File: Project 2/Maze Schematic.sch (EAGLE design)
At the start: 29 parts, among them SW1 BUTTON, SW2 BUTTON, SW3 BUTTON, SW4 BUTTON, SW5 BUTTON, U1 MOD-LED8X8RGB-CONN, U2 MPU-9250, U3 POCKETBEAGLE, U6 MOD-LED8X8RGB-CONN

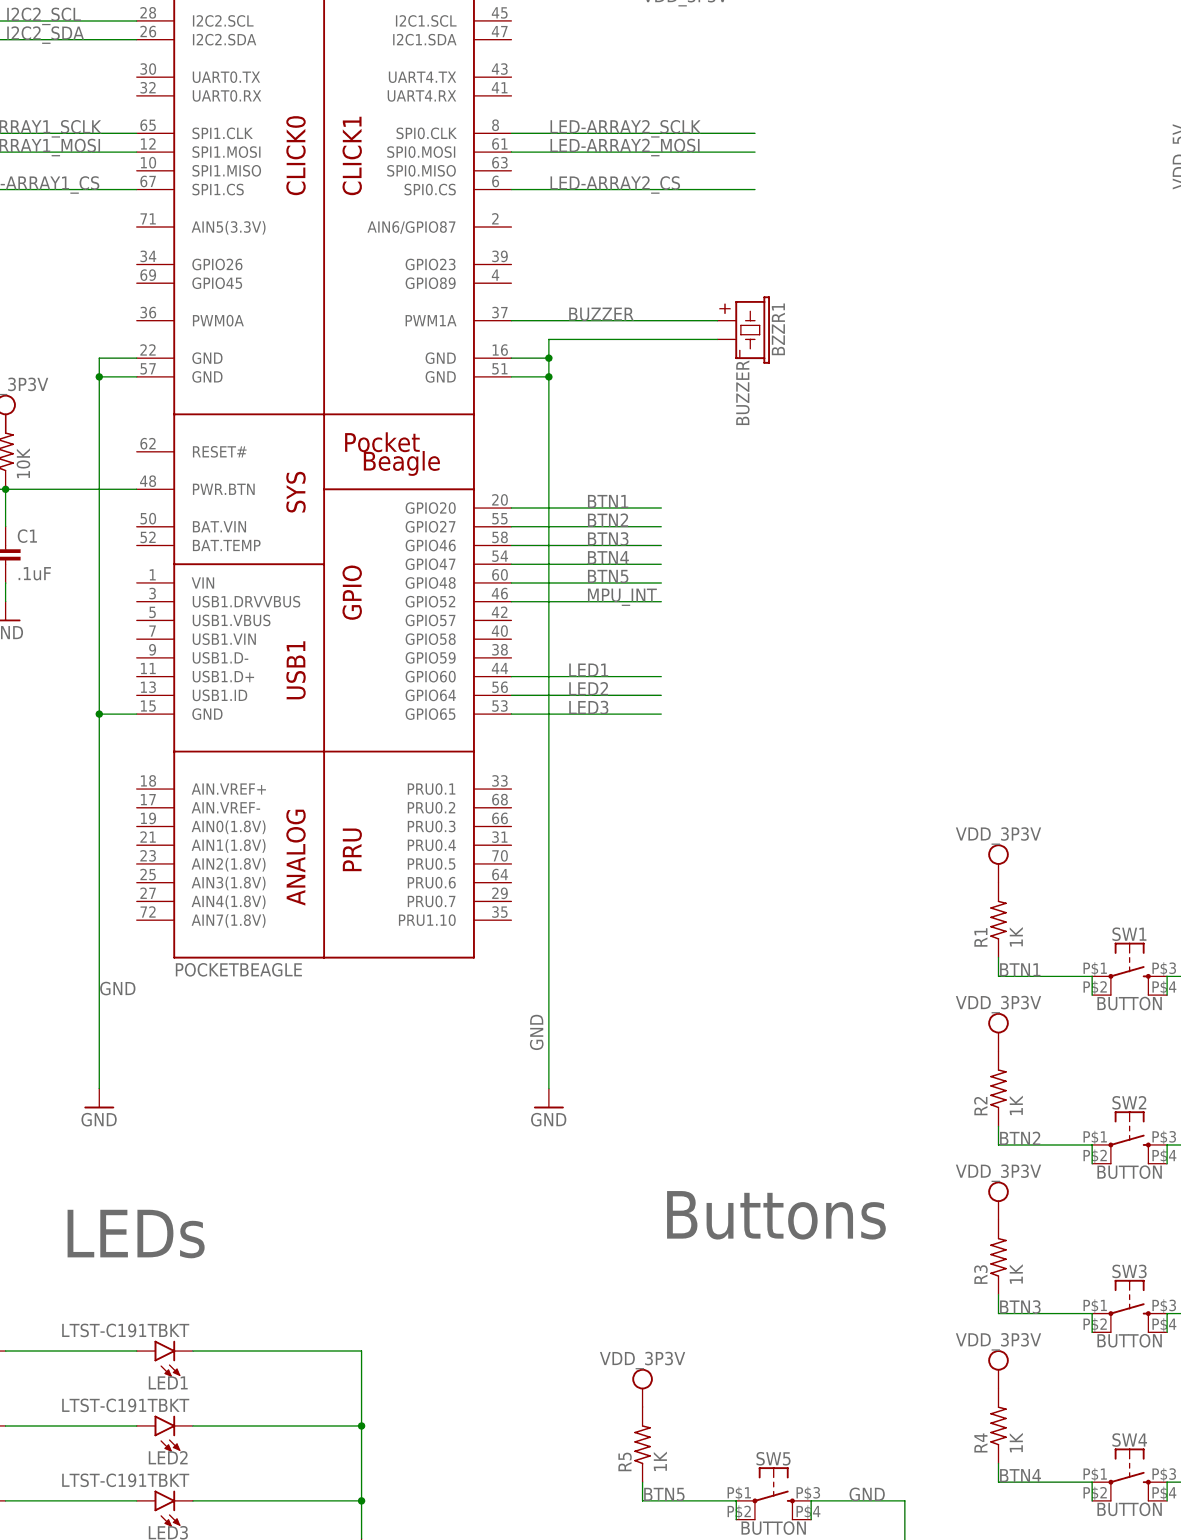
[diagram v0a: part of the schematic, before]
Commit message: Began routing and updated pocket beagle device
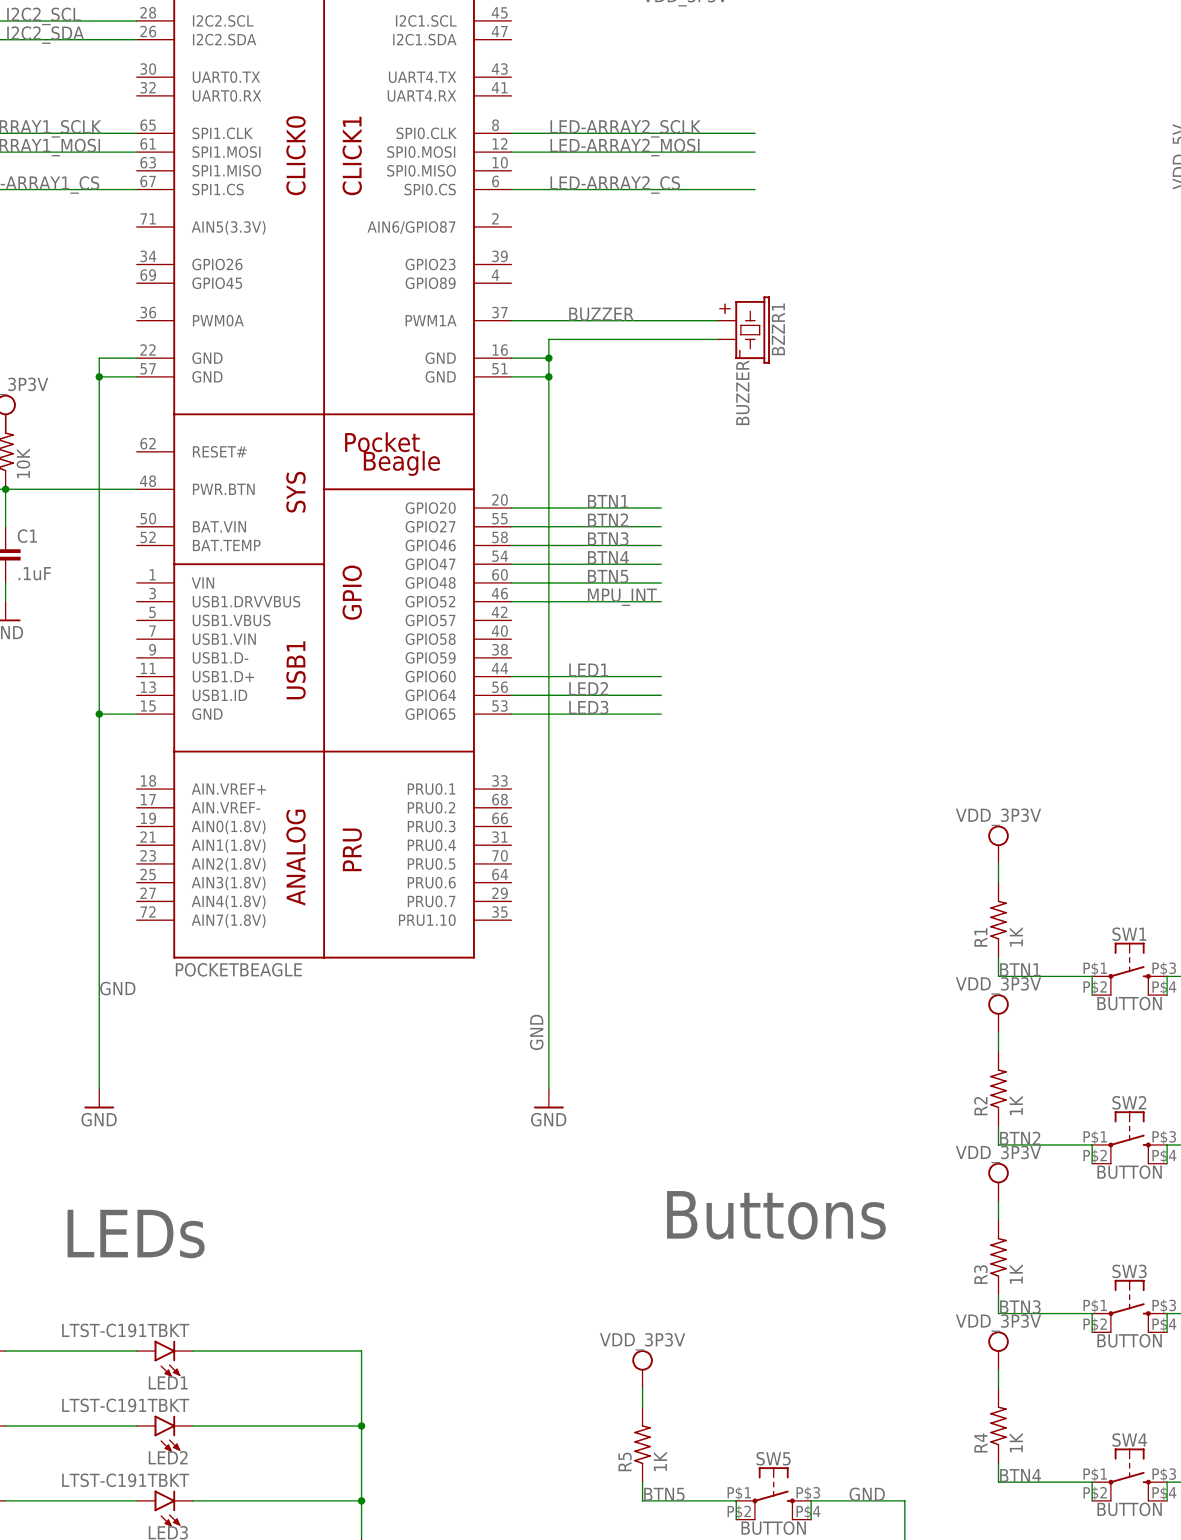
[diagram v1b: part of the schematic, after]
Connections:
- removed net SYS_VDD1_3P3V: R1.2, R2.2, R3.2, R4.2, R5.2
- net VDD_3P3V: now also R1.2, R2.2, R3.2, R4.2, R5.2
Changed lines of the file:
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@@
 <instance part="U6" gate="G$1" x="261.62" y="205.74"/>
 <instance part="GND2" gate="1" x="223.52" y="81.28"/>
-<instance part="SUPPLY2" gate="G$1" x="187.96" y="106.68"/>
+<instance part="SUPPLY2" gate="G$1" x="187.96" y="109.22"/>
 <instance part="SW1" gate="G$1" x="205.74" y="91.44"/>
 <instance part="R1" gate="G$1" x="187.96" y="99.06" rot="R90"/>
 <instance part="GND1" gate="1" x="223.52" y="58.42"/>
-<instance part="SUPPLY1" gate="G$1" x="187.96" y="83.82"/>
+<instance part="SUPPLY1" gate="G$1" x="187.96" y="86.36"/>
 <instance part="SW2" gate="G$1" x="205.74" y="68.58"/>
 <instance part="R2" gate="G$1" x="187.96" y="76.2" rot="R90"/>
 <instance part="GND3" gate="1" x="223.52" y="35.56"/>
-<instance part="SUPPLY3" gate="G$1" x="187.96" y="60.96"/>
+<instance part="SUPPLY3" gate="G$1" x="187.96" y="63.5"/>
 <instance part="SW3" gate="G$1" x="205.74" y="45.72"/>
 <instance part="R3" gate="G$1" x="187.96" y="53.34" rot="R90"/>
 <instance part="GND4" gate="1" x="223.52" y="12.7"/>
-<instance part="SUPPLY4" gate="G$1" x="187.96" y="38.1"/>
+<instance part="SUPPLY4" gate="G$1" x="187.96" y="40.64"/>
 <instance part="SW4" gate="G$1" x="205.74" y="22.86"/>
 <instance part="R4" gate="G$1" x="187.96" y="30.48" rot="R90"/>
 <instance part="GND5" gate="1" x="175.26" y="10.16"/>
-<instance part="SUPPLY5" gate="G$1" x="139.7" y="35.56"/>
+<instance part="SUPPLY5" gate="G$1" x="139.7" y="38.1"/>
 <instance part="SW5" gate="G$1" x="157.48" y="20.32"/>
 <instance part="R5" gate="G$1" x="139.7" y="27.94" rot="R90"/>
@@
 </segment>
 </net>
-<net name="SYS_VDD1_3P3V" class="0">
-<segment>
-<pinref part="SUPPLY2" gate="G$1" pin="SYS_VDD1_3P3V"/>
-<pinref part="R1" gate="G$1" pin="2"/>
-</segment>
-<segment>
-<pinref part="SUPPLY1" gate="G$1" pin="SYS_VDD1_3P3V"/>
-<pinref part="R2" gate="G$1" pin="2"/>
-</segment>
-<segment>
-<pinref part="SUPPLY3" gate="G$1" pin="SYS_VDD1_3P3V"/>
-<pinref part="R3" gate="G$1" pin="2"/>
-</segment>
-<segment>
-<pinref part="SUPPLY4" gate="G$1" pin="SYS_VDD1_3P3V"/>
-<pinref part="R4" gate="G$1" pin="2"/>
-</segment>
-<segment>
-<pinref part="SUPPLY5" gate="G$1" pin="SYS_VDD1_3P3V"/>
-<pinref part="R5" gate="G$1" pin="2"/>
-</segment>
-</net>
 <net name="BTN2" class="0">
 <segment>
@@
 <label x="264.16" y="116.84" size="1.778" layer="95"/>
 </segment>
-</net>
+<segment>
+<pinref part="SUPPLY3" gate="G$1" pin="SYS_VDD1_3P3V"/>
+<pinref part="R3" gate="G$1" pin="2"/>
+<wire x1="187.96" y1="60.96" x2="187.96" y2="58.42" width="0.1524" layer="91"/>
+</segment>
+<segment>
+<pinref part="SUPPLY4" gate="G$1" pin="SYS_VDD1_3P3V"/>
+<pinref part="R4" gate="G$1" pin="2"/>
+<wire x1="187.96" y1="38.1" x2="187.96" y2="35.56" width="0.1524" layer="91"/>
+</segment>
+<segment>
+<pinref part="SUPPLY1" gate="G$1" pin="SYS_VDD1_3P3V"/>
+<pinref part="R2" gate="G$1" pin="2"/>
+<wire x1="187.96" y1="83.82" x2="187.96" y2="81.28" width="0.1524" layer="91"/>
+</segment>
+<segment>
+<pinref part="SUPPLY2" gate="G$1" pin="SYS_VDD1_3P3V"/>
+<pinref part="R1" gate="G$1" pin="2"/>
+<wire x1="187.96" y1="106.68" x2="187.96" y2="104.14" width="0.1524" layer="91"/>
+</segment>
+<segment>
+<pinref part="SUPPLY5" gate="G$1" pin="SYS_VDD1_3P3V"/>
+<pinref part="R5" gate="G$1" pin="2"/>
+<wire x1="139.7" y1="35.56" x2="139.7" y2="33.02" width="0.1524" layer="91"/>
+</segment>
+</net>

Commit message: Completed board routing
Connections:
- net N$1 renamed REGOUT
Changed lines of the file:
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@@
 </segment>
 </net>
-<net name="N$1" class="0">
+<net name="REGOUT" class="0">
 <segment>
 <pinref part="U2" gate="G$1" pin="REGOUT"/>

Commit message: Added Documentation and mounting holes, as well as a pdf version of board and schematic
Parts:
- added MGT1, MGT2, MGT3, MGT4, MGT5, MGT6: MOUNTING_HOLE, Buzzer Box:MOUNTING_HOLE
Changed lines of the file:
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@@
 <?xml version="1.0" encoding="utf-8"?>
 <!DOCTYPE eagle SYSTEM "eagle.dtd">
-<eagle version="8.7.1">
+<eagle version="9.0.0">
 <drawing>
 <settings>
-<setting alwaysvectorfont="no"/>
+<setting alwaysvectorfont="yes"/>
 <setting verticaltext="up"/>
 </settings>
@@
 <part name="R10" library="Buzzer Box" deviceset="R_" device="R0603" value="1K"/>
 <part name="R11" library="Buzzer Box" deviceset="R_" device="R0603" value="1K"/>
+<part name="MGT1" library="Buzzer Box" deviceset="MOUNTING_HOLE" device=""/>
+<part name="MGT2" library="Buzzer Box" deviceset="MOUNTING_HOLE" device=""/>
+<part name="MGT3" library="Buzzer Box" deviceset="MOUNTING_HOLE" device=""/>
+<part name="MGT4" library="Buzzer Box" deviceset="MOUNTING_HOLE" device=""/>
+<part name="MGT5" library="Buzzer Box" deviceset="MOUNTING_HOLE" device=""/>
+<part name="MGT6" library="Buzzer Box" deviceset="MOUNTING_HOLE" device=""/>
 </parts>
 <sheets>
@@
 <instance part="R10" gate="G$1" x="25.4" y="228.6" rot="R90"/>
 <instance part="R11" gate="G$1" x="15.24" y="228.6" rot="R90"/>
+<instance part="MGT1" gate="G$1" x="167.64" y="154.94"/>
+<instance part="MGT2" gate="G$1" x="180.34" y="154.94"/>
+<instance part="MGT3" gate="G$1" x="193.04" y="154.94"/>
+<instance part="MGT4" gate="G$1" x="205.74" y="154.94"/>
+<instance part="MGT5" gate="G$1" x="167.64" y="137.16"/>
+<instance part="MGT6" gate="G$1" x="180.34" y="137.16"/>
 </instances>
 <busses>
